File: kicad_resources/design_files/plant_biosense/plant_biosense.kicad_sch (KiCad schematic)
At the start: 74 parts, among them J1 RJ45_Shielded, J2 RJ45_Shielded, U1 LM7805_TO220, U10 OP07, U11 TXS0108EPW, U12 OP07, U13 TL081, U14 NodeMCU1.0(ESP-12E), U15 ADS1115IDGS, U2 CD4051B, U3 CD4051B, U4 2S4P LI-ION BATTERY, U5 2S LI-ION BMS 10A, U6 2S LI-ION CC/CV CHARGER, U7 XL4015, U8 AD620_instrumentation_amplifi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, U9 INA219AxD

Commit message: Initial public release: add CHL, docs, schematics
Adds CEREPHYTE Hardware License (CHL v1.0), NOTICE, CHANGELOG and THIRD_PARTY attribution; updates README. Adds multiple schematic PDFs under SCHEMATICS. Updates KiCad plant_biosense files (rev 4.2): date/revision bump, net/pad fixes (Net-(A1-D13)), pin type change, netclass/property and several wiring/no_connect adjustments. Prepares repository for public release and clarifies third-party licensing for included kicad-ESP8266 files.
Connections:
- net at A1.26 (D11), J2.6: no longer J2.3
- net at A1.28 (D13): now also J2.3
- no-connect marks 42 -> 41
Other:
- note added: "POWER SUPPLY UNIT +5v linear and buck"
- note removed: "POWER SUPPLY UNIT"
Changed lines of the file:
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@@
 	(title_block
 		(title "CEREPHYTE\n")
-		(date "2026-06-12")
-		(rev "4")
+		(date "2026-08-03")
+		(rev "4.2")
 		(company "ISLERI")
 	)
@@
 		)
 	)
-	(text "POWER SUPPLY UNIT"
+	(text "POWER SUPPLY UNIT +5v linear and buck"
 		(exclude_from_sim no)
-		(at 23.114 115.316 0)
+		(at 31.242 115.062 0)
 		(effects
 			(font
@@
 	)
 	(junction
-		(at 99.06 93.98)
-		(diameter 0)
-		(color 0 0 0 0)
-	)
-	(junction
 		(at 35.56 52.07)
 		(diameter 0)
@@
 	)
 	(no_connect
-		(at 165.1 114.3)
-	)
-	(no_connect
 		(at 256.54 153.67)
 	)
@@
 	(wire
 		(pts
+			(xy 106.68 92.71) (xy 106.68 96.52)
+		)
+		(stroke
+			(width 0)
+			(type default)
+		)
+	)
+	(wire
+		(pts
 			(xy 139.7 157.48) (xy 146.05 157.48)
 		)
@@
 	(wire
 		(pts
+			(xy 151.13 111.76) (xy 165.1 111.76)
+		)
+		(stroke
+			(width 0)
+			(type default)
+		)
+	)
+	(wire
+		(pts
 			(xy 224.79 49.53) (xy 224.79 57.15)
 		)
@@
 	(wire
 		(pts
-			(xy 106.68 93.98) (xy 106.68 96.52)
-		)
-		(stroke
-			(width 0)
-			(type default)
-		)
-	)
-	(wire
-		(pts
 			(xy 38.1 92.71) (xy 34.29 92.71)
 		)
@@
 	(wire
 		(pts
+			(xy 151.13 92.71) (xy 151.13 111.76)
+		)
+		(stroke
+			(width 0)
+			(type default)
+		)
+	)
+	(wire
+		(pts
 			(xy 19.05 26.67) (xy 21.59 26.67)
 		)
@@
 	(wire
 		(pts
-			(xy 165.1 114.3) (xy 165.1 111.76)
-		)
-		(stroke
-			(width 0)
-			(type default)
-		)
-	)
-	(wire
-		(pts
 			(xy 97.79 12.7) (xy 97.79 19.05)
 		)
@@
 	(wire
 		(pts
-			(xy 99.06 96.52) (xy 99.06 93.98)
+			(xy 106.68 92.71) (xy 151.13 92.71)
 		)
 		(stroke
@@
 	(wire
 		(pts
-			(xy 102.87 154.94) (xy 92.71 154.94)
+			(xy 99.06 91.44) (xy 99.06 96.52)
 		)
 		(stroke
@@
 	(wire
 		(pts
-			(xy 91.44 72.39) (xy 96.52 72.39)
+			(xy 102.87 154.94) (xy 92.71 154.94)
 		)
 		(stroke
@@
 	(wire
 		(pts
-			(xy 152.4 106.68) (xy 152.4 91.44)
+			(xy 91.44 72.39) (xy 96.52 72.39)
 		)
 		(stroke
@@
 	(wire
 		(pts
-			(xy 62.23 25.4) (xy 62.23 48.26)
+			(xy 152.4 106.68) (xy 152.4 91.44)
 		)
 		(stroke
@@
 	(wire
 		(pts
-			(xy 266.7 40.64) (xy 266.7 49.53)
+			(xy 62.23 25.4) (xy 62.23 48.26)
 		)
 		(stroke
@@
 	(wire
 		(pts
-			(xy 86.36 19.05) (xy 97.79 19.05)
+			(xy 266.7 40.64) (xy 266.7 49.53)
 		)
 		(stroke
@@
 	(wire
 		(pts
-			(xy 99.06 91.44) (xy 99.06 93.98)
+			(xy 86.36 19.05) (xy 97.79 19.05)
 		)
 		(stroke
@@
 	(wire
 		(pts
-			(xy 99.06 93.98) (xy 106.68 93.98)
-		)
-		(stroke
-			(width 0)
-			(type default)
-		)
-	)
-	(wire
-		(pts
 			(xy 276.86 31.75) (xy 255.27 31.75)
 		)
@@
 			(show_name no)
 			(do_not_autoplace no)
+			(effects
+				(font
+					(size 1.27 1.27)
+					(italic yes)
+				)
+			)
+		)
+	)
+	(netclass_flag ""
+		(length 2.54)
+		(shape round)
+		(at 133.35 92.71 180)
+		(fields_autoplaced yes)
+		(effects
+			(font
+				(size 1.27 1.27)
+			)
+			(justify right bottom)
+		)
+		(property "Net Class" "Digital_IO"
+			(at 134.0485 95.25 0)
+			(hide yes)
+			(show_name no)
+			(do_not_autoplace no)
+			(effects
+				(font
+					(size 1.27 1.27)
+				)
+				(justify left)
+			)
+		)
+		(property "Component Class" ""
+			(at 68.58 6.35 0)
+			(show_name no)
+			(do_not_autoplace no)

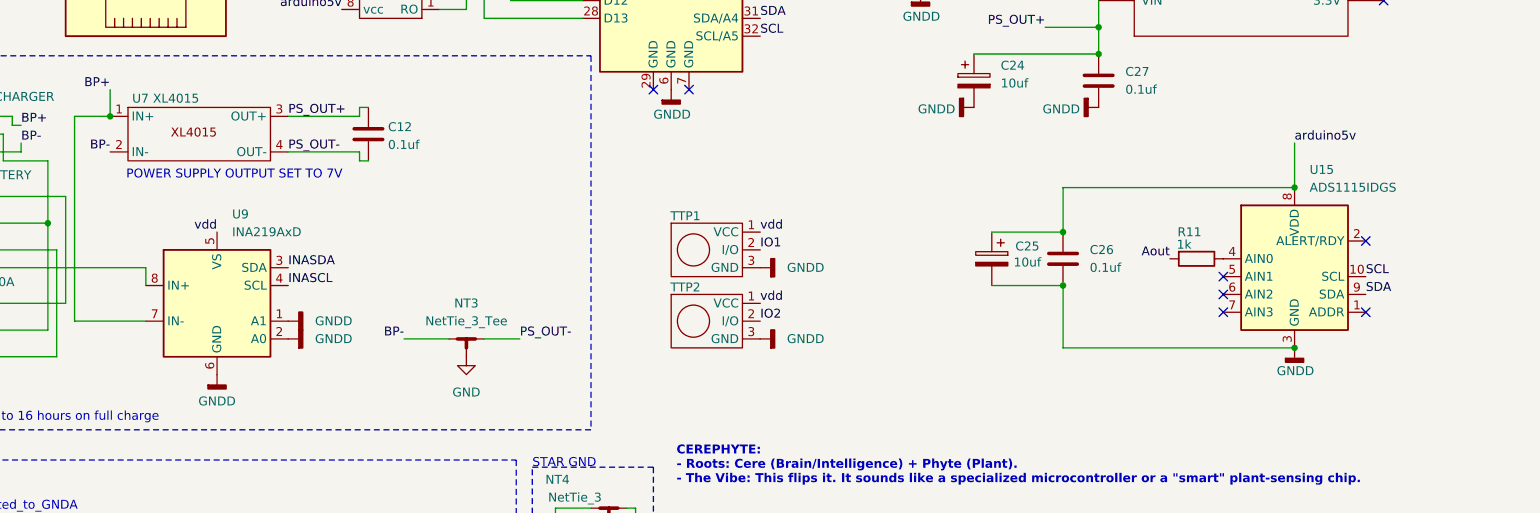
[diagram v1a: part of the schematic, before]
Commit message: Improve biosense BOM and schematic layout
Updated the Plant Biosense BOM with KiCad export fields, datasheet links, and corrected component metadata. Refreshed the designator list in the project file and adjusted the schematic layout by moving the XL4015 output note, adding a capacitive touch interface annotation, and aligning related symbols and wiring for a cleaner design.
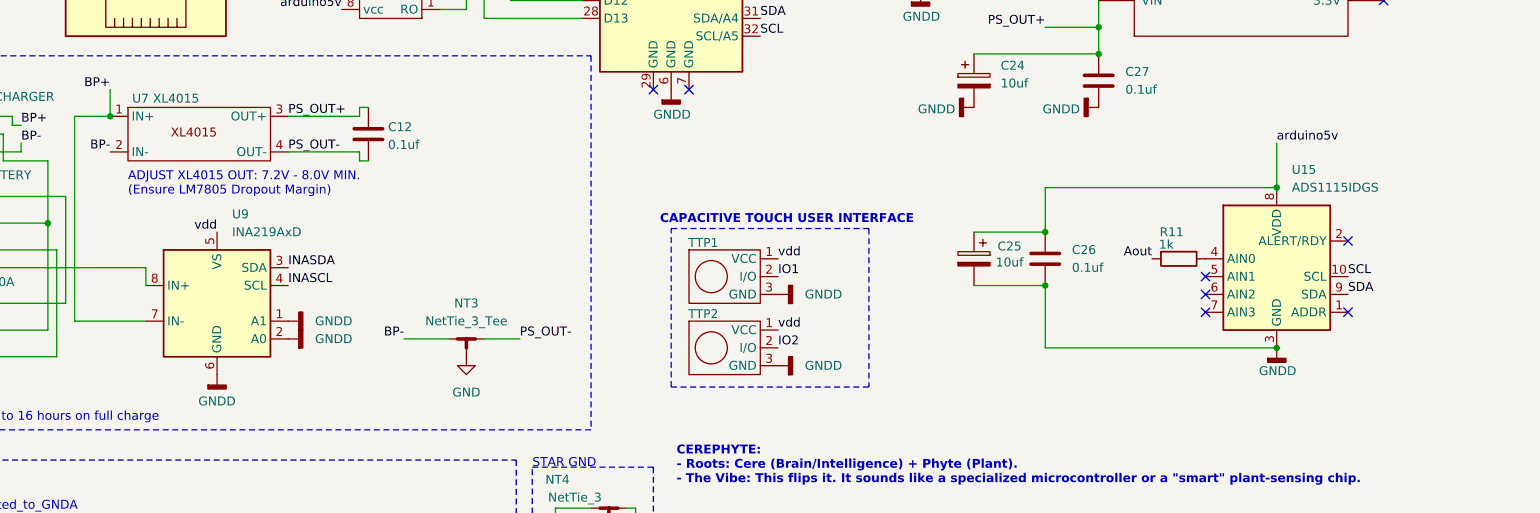
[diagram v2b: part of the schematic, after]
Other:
- note added: "ADJUST XL4015 OUT: 7.2V - 8.0V MIN. (Ensure LM7805 Dropout Margin)"
- note added: "CAPACITIVE TOUCH USER INTERFACE"
- note removed: "POWER SUPPLY OUTPUT SET TO 7V"
- moved on the sheet: C25, C26, R11, TTP1, TTP2, U15

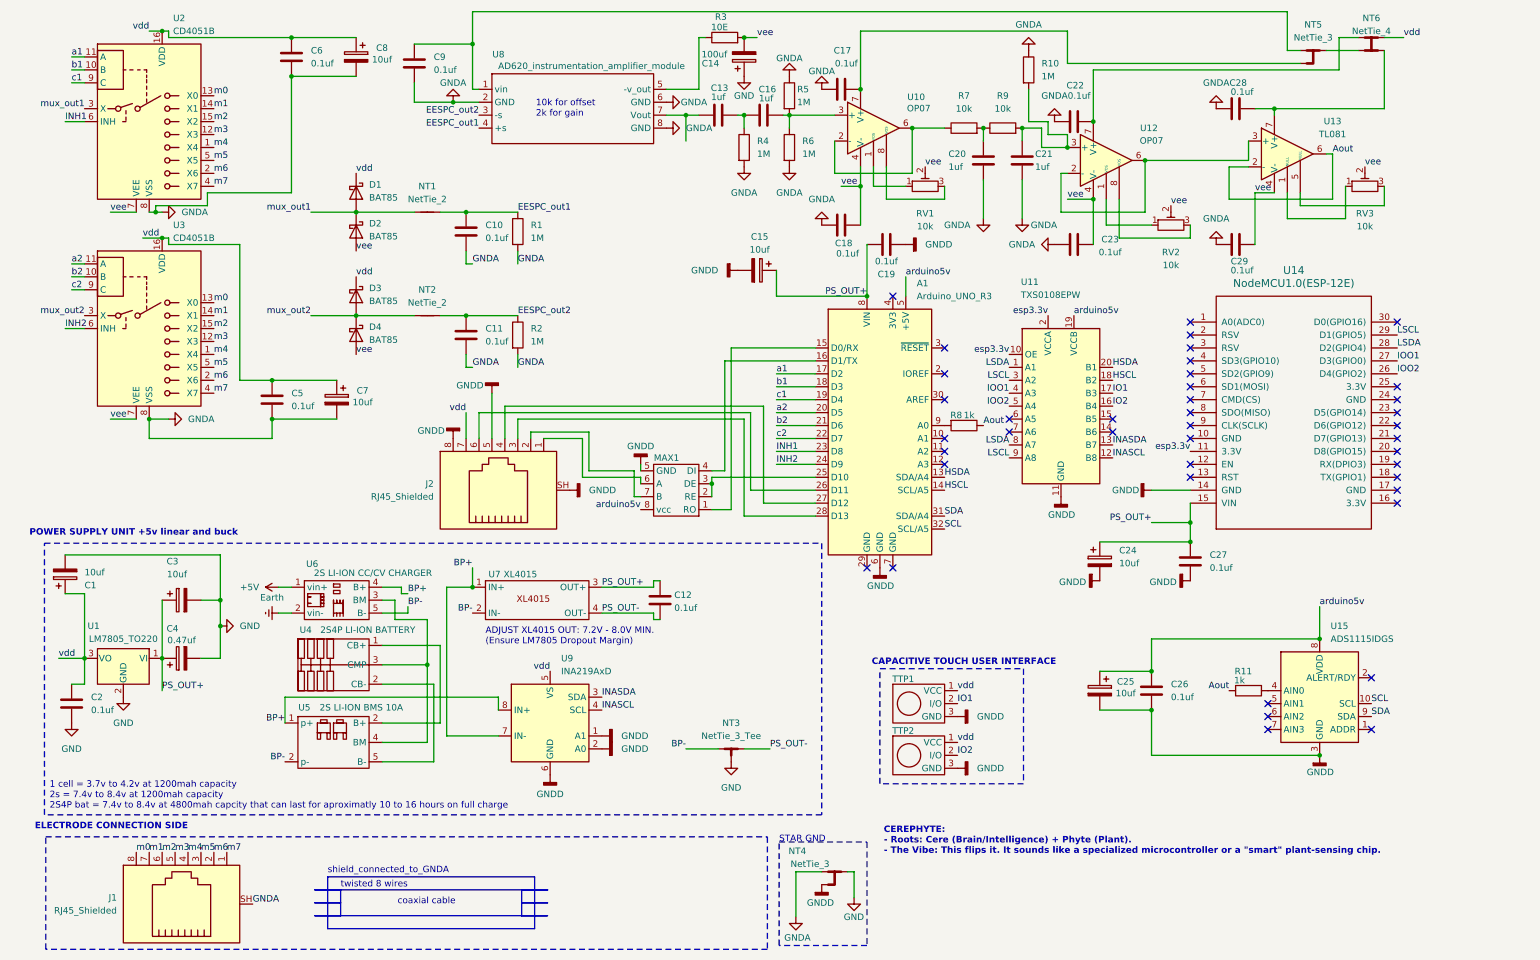
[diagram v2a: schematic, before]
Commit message: 16 october 2026
Finalize CEREPHYTE Rev. 4.2 schematic architecture

- Finalize power supply, analog front-end, ADC, and microcontroller architecture
- Configure XL4015 buck converter for regulated 5V VDD
- Document INA219 and ADS1115 I2C addresses
- Define split analog/digital grounding topology
- Prepare schematic for physical protoboard implementation

Author: Omm Prakash Das
Date: 2026-10-16
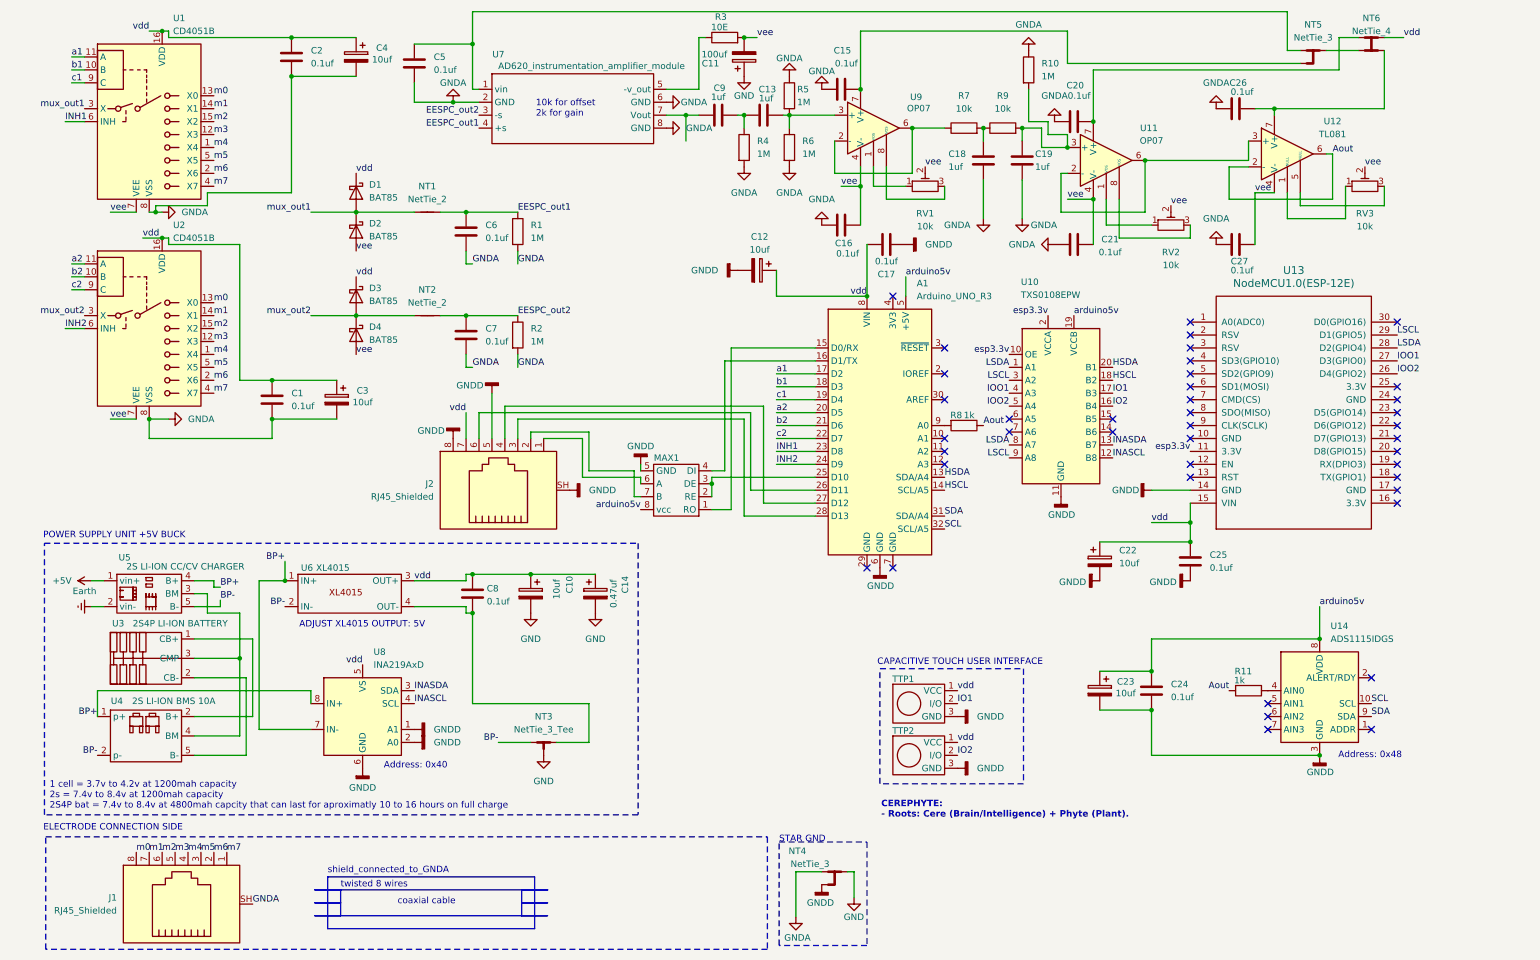
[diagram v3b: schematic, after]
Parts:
- removed C1, C3: 10uf, Capacitor_THT:CP_Radial_D5.0mm_P2.00mm, symbol Device:C_Polarized
- removed C2: 0.1uf, Capacitor_THT:C_Disc_D5.0mm_W2.5mm_P2.50mm, symbol Device:C
- removed C4: 0.47uf, Capacitor_THT:CP_Radial_D5.0mm_P2.00mm, symbol Device:C_Polarized
- removed U1: LM7805_TO220, Package_TO_SOT_THT:TO-220-3_Vertical, symbol Regulator_Linear:LM7805_TO220
- added C10: 10uf, Capacitor_THT:CP_Radial_D5.0mm_P2.00mm, symbol Device:C_Polarized
- added C14: 0.47uf, Capacitor_THT:CP_Radial_D5.0mm_P2.00mm, symbol Device:C_Polarized
- renumbered C5 to C1, C14 to C11, C15 to C12, C16 to C13, C17 to C15, C18 to C16, C19 to C17, C20 to C18, C21 to C19, C6 to C2, C22 to C20, C23 to C21, C24 to C22, C25 to C23, C26 to C24, C27 to C25, C28 to C26, C29 to C27, C7 to C3, C8 to C4, C9 to C5, C10 to C6, C11 to C7, C12 to C8, C13 to C9, U2 to U1, U11 to U10, U12 to U11, U13 to U12, U14 to U13, U15 to U14, U3 to U2, U4 to U3, U5 to U4, U6 to U5, U7 to U6, U8 to U7, U9 to U8, U10 to U9
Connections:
- net PS_OUT+ is gone; now on net vdd: A1.8 (VIN), C12.1, C17.1, C22.1, C25.1, C8.1, U13.15 (VIN), U6.3 (OUT+)
- net GND: now also C10.2, C14.2
- net vdd: now also C10.1, C14.1
- net PS_OUT-: no longer names the net of C8.2, NT3.2, U6.4 (OUT-)
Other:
- note added: "ADJUST XL4015 OUTPUT: 5V"
- note added: "Address: 0x40"
- note added: "Address: 0x48"
- note added: "CEREPHYTE: - Roots: Cere (Brain/Intelligence) + Phyte (Plant)."
- note added: "POWER SUPPLY UNIT +5V BUCK"
- note removed: "ADJUST XL4015 OUT: 7.2V - 8.0V MIN. (Ensure LM7805 Dropout Margin)"
- note removed: "CEREPHYTE: - Roots: Cere (Brain/Intelligence) + Phyte (Plant). - The Vibe: This flips it. It sounds like a specialized microcontroller or a "smart" plant-sensing chip."
- note removed: "POWER SUPPLY UNIT +5v linear and buck"
- moved on the sheet: C8, NT3, U3, U4, U5, U6, U8
